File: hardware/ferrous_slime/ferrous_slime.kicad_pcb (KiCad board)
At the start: 2 copper layers, 41.4 x 34 mm, 50 parts, among them J1 IMU_Connector, J2 Battery_Connector, J3 USB_C_Receptacle_USB2.0, Q1 DMG3415U, SW1 SW_PWR, U1 BNO/MPU/ICM_Break, U2 ESP32-C3-MINI-1, U3 TP4056, U4 M3406, Y1 32.768Hz

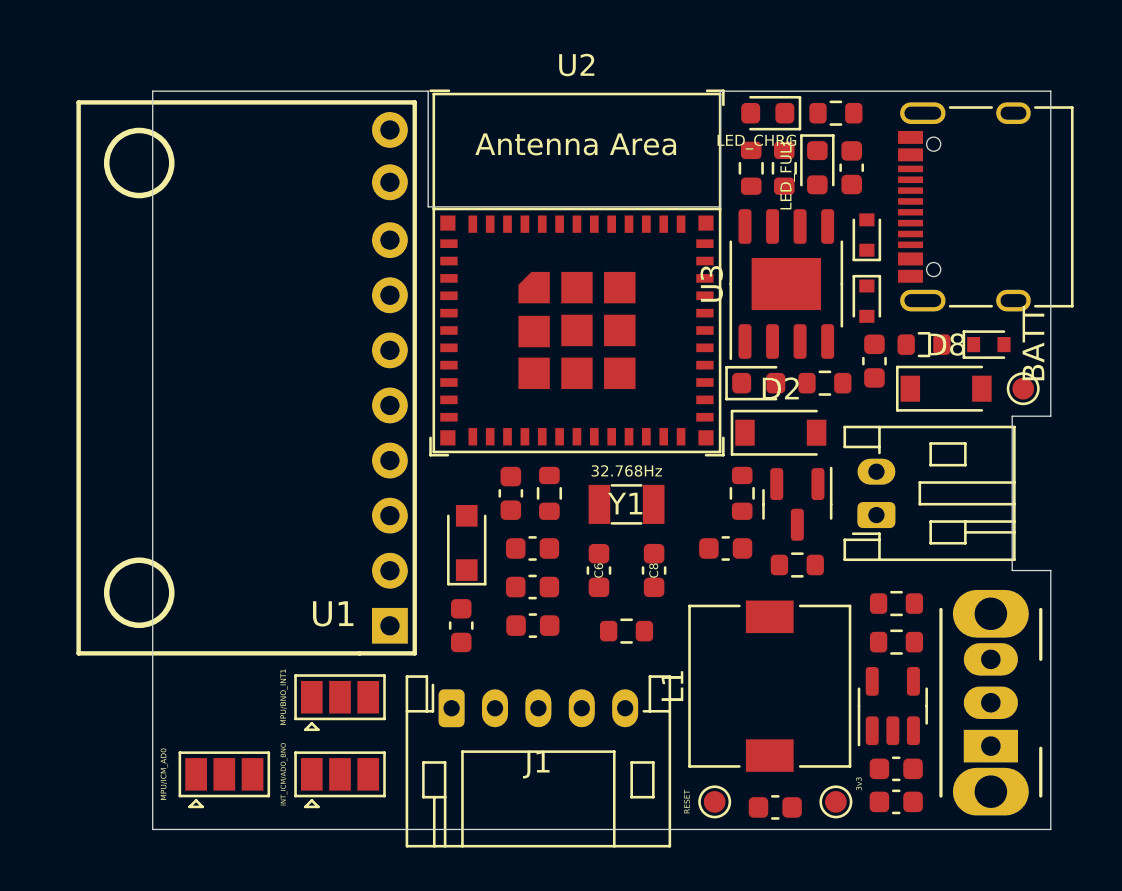
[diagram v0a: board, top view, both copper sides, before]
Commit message: Routed all nets, fixed most of silkscreen
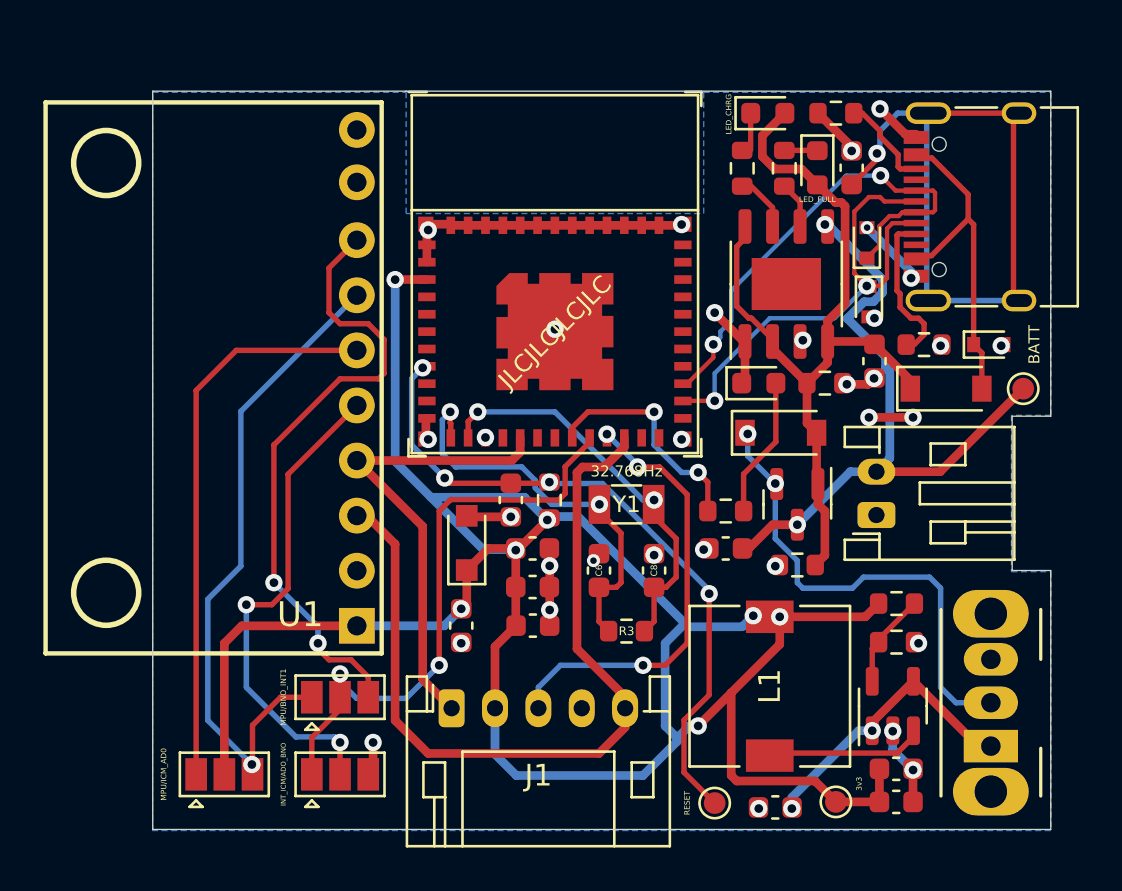
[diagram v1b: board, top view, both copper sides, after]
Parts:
- C7, C9: value 10u -> 10uF
- D5: value LED -> PROG_LED
- moved U1 1.52 mm to (58.4, 43.1)
- moved R7 1.12 mm to (82.0, 49.3), turned to 0 degrees
- moved U2 1.02 mm to (74.2, 41.0)
- moved R5 0.41 mm to (82.8, 33.5)
- moved D7 0.36 mm to (88.6, 36.9)
- moved C2 0.31 mm to (72.1, 48.8)
- moved R1 0.31 mm to (73.9, 48.8)
- moved J3 0.25 mm to (94.5, 35.3)
- moved D6 0.10 mm to (88.6, 39.6)
- moved TP1 0.05 mm to (81.5, 62.7)
- turned C9 to 180 degrees
- turned D3 to 0 degrees
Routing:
- net +3V3: track 0.00 -> 109.8 mm, vias 0 -> 7
- net GND: track 0.00 -> 63.5 mm, vias 0 -> 32
- net VBUS: track 0.00 -> 37.0 mm
- net IO8_SCL: track 0.00 -> 37.0 mm
- net Net-(C2-Pad1): track 0.00 -> 31.1 mm, vias 0 -> 4
- net Net-(JP1-Pad3): track 0.00 -> 30.9 mm, vias 0 -> 1
- net Net-(C10-Pad1): track 0.00 -> 30.8 mm, vias 0 -> 1
- net +BATT: track 0.00 -> 30.6 mm, vias 0 -> 2
- net Net-(JP3-Pad3): track 0.00 -> 29.0 mm, vias 0 -> 2
- net Net-(JP1-Pad1): track 0.00 -> 25.9 mm
- net IO6_INT1: track 0.00 -> 25.5 mm, vias 0 -> 2
- net Net-(JP2-Pad2): track 0.00 -> 22.6 mm, vias 0 -> 2
- net USB_D-: track 0.00 -> 22.6 mm, vias 0 -> 2
- net USB_D+: track 0.00 -> 22.2 mm, vias 0 -> 2
- net Net-(D2-Pad1): track 0.00 -> 22.1 mm, vias 0 -> 2
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- added copper zone on B.Cu, net GND
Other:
- outline, holes or cut-outs redrawn
- board text added: "JLCJLCJLCJLC"
- board text added: "License: CERN-OHL-P v2 or later github.com/TheButlah/slimevr_pcb"
